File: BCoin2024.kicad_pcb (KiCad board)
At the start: 2 copper layers, 50 x 50 mm, 21 parts, among them U1 NE555DR, U2 74HC4017D_653

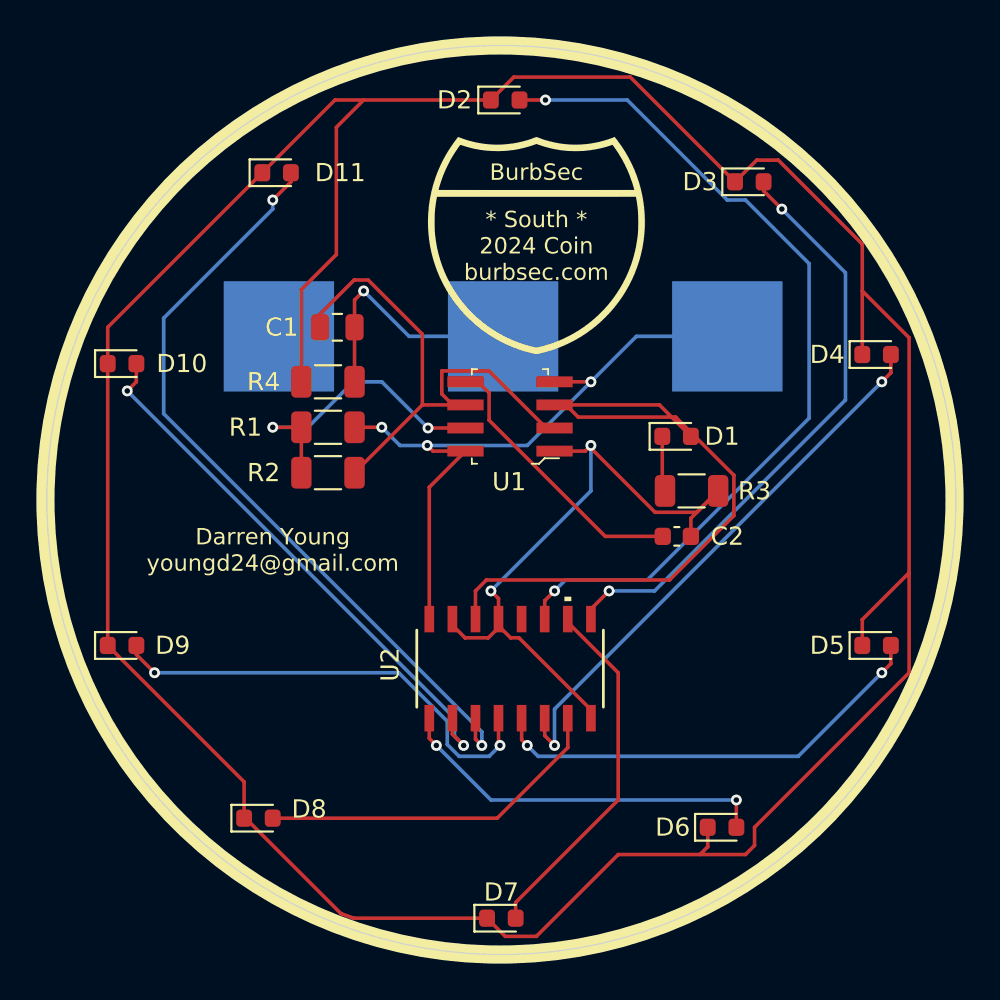
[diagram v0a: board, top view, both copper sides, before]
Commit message: added datasheets
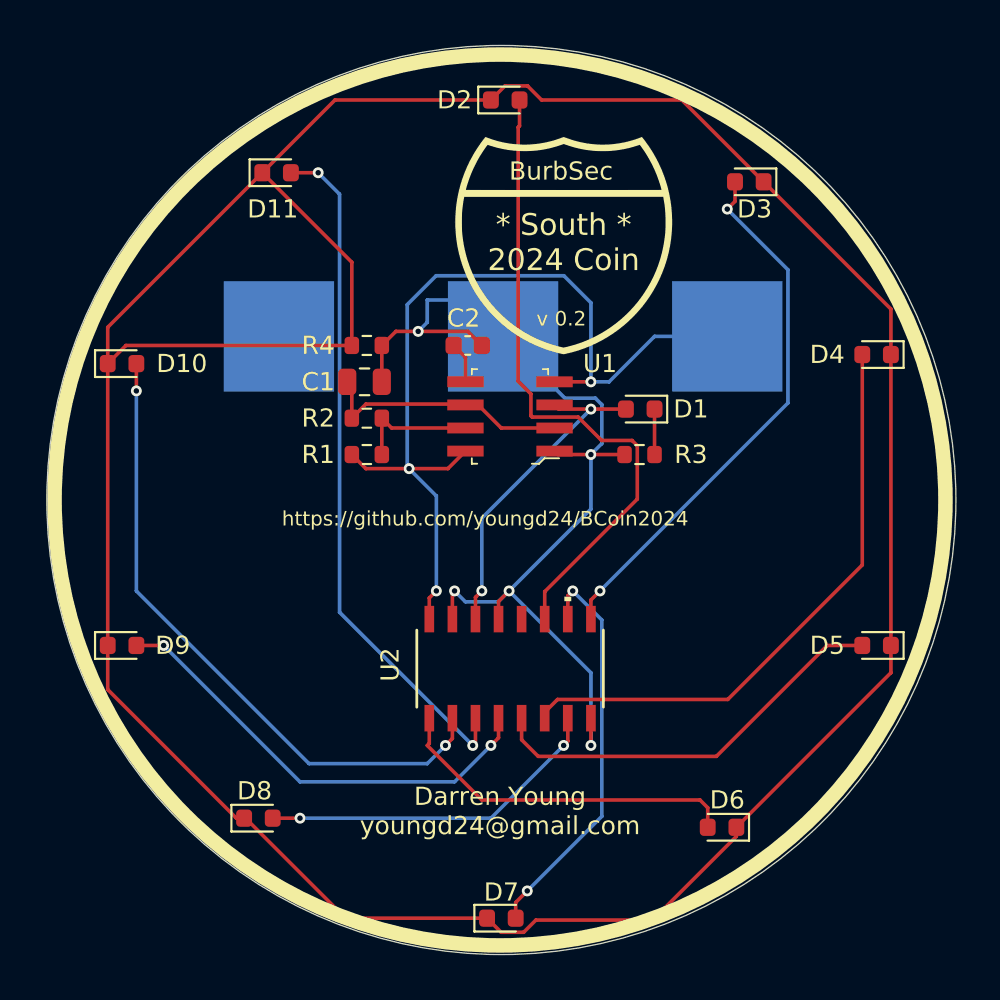
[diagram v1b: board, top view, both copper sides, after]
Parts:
- R1, R2, R3, R4: footprint Resistor_SMD:R_1206_3216Metric -> Resistor_SMD:R_0603_1608Metric
- moved C2 15.6 mm to (132.7, 81.5)
- moved R2 3.68 mm to (127.2, 85.5), turned to 180 degrees
- moved R3 3.49 mm to (142.2, 87.5), turned to 180 degrees
- moved C1 3.35 mm to (127.0, 83.5)
- moved R4 2.93 mm to (127.2, 81.5)
- moved R1 2.61 mm to (127.2, 87.5), turned to 0 degrees
- moved D1 2.50 mm to (142.2, 85.0), turned to 180 degrees
- moved G*** 1.50 mm to (138.0, 76.0)
- turned D3 to 180 degrees
- turned D4 to 180 degrees
- turned D5 to 180 degrees
- turned D6 to 180 degrees
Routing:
- net Net-(D1-A): track 39.4 -> 18.2 mm, vias 0 -> 2
- net Net-(U1-THRES): track 30.2 -> 14.1 mm
- net VCC: track 37.7 -> 51.4 mm
- net Net-(U1-CONT): track 15.3 -> 2.27 mm
- net Net-(D2-A): track 47.9 -> 35.9 mm, vias 2 -> 0
- net Net-(U1-DISCH): track 16.8 -> 6.82 mm, vias 2 -> 0
- net Net-(D10-K): track 179.7 -> 173.6 mm
- net Net-(D11-A): track 43.3 -> 38.1 mm
- net GND: track 51.9 -> 57.1 mm, vias 3 -> 5
- net Net-(D10-A): track 30.6 -> 35.5 mm
- net Net-(D3-A): track 33.2 -> 30.1 mm
- net Net-(D7-A): track 19.9 -> 22.3 mm, vias 0 -> 2
- net Net-(D5-A): track 25.0 -> 22.8 mm, vias 2 -> 0
- net Net-(D4-A): track 30.9 -> 32.7 mm, vias 2 -> 0
- net Net-(D6-A): track 20.9 -> 19.5 mm, vias 2 -> 0
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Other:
- board text added: "* South * 2024 Coin"
- board text added: "https://github.com/youngd24/BCoin2024"
- board text added: "v 0.2"
- board text removed: "* South * 2024 Coin burbsec.com"

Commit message: added assets and images
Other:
- board text added: "v0.2"
- board text removed: "v 0.2"
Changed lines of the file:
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@@
 		)
 	)
-	(gr_text "v 0.2"
+	(gr_text "v0.2"
 		(at 136.5 80.5 0)
 		(layer "F.SilkS")

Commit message: Version 0.3
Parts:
- added C3: 10nF, Capacitor_SMD:C_0603_1608Metric, F.Cu at (142.0, 86.0)
- moved G*** 3.50 mm to (134.5, 76.0)
- moved D1 2.76 mm to (142.0, 87.8)
- moved U2 2.56 mm to (134.8, 96.7)
- moved U1 2.29 mm to (134.6, 87.6)
- moved C1 2.23 mm to (127.0, 85.7)
- moved C2 2.23 mm to (132.7, 83.7)
- moved R2 2.23 mm to (127.2, 87.7)
- moved R4 2.23 mm to (127.2, 83.7)
- moved R3 2.00 mm to (142.1, 89.5)
- moved R1 2.00 mm to (127.2, 89.5)
- moved BT1 1.00 mm to (134.7, 80.0)
- moved D2 0.50 mm to (134.8, 67.5)
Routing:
- net VCC: track 51.4 -> 36.7 mm, vias 3 -> 6
- net Net-(D7-A): track 22.3 -> 31.6 mm
- net Net-(D2-A): track 35.9 -> 29.9 mm, vias 0 -> 2
- net GND: track 57.1 -> 51.4 mm, vias 5 -> 3
- net Net-(D3-A): track 30.1 -> 25.5 mm
- net Net-(D8-A): track 19.3 -> 23.8 mm
- net Net-(D10-A): track 35.5 -> 31.8 mm
- net Net-(D1-A): track 18.2 -> 14.8 mm
- net Net-(D11-A): track 38.1 -> 34.7 mm
- net Net-(D5-A): track 22.8 -> 24.9 mm, vias 0 -> 2
- net Net-(D6-A): track 19.5 -> 21.1 mm, vias 0 -> 2
- net Net-(D9-A): track 25.1 -> 23.9 mm
- net Net-(D10-K): track 173.6 -> 172.6 mm, vias 0 -> 11
- net Net-(U1-DISCH): track 6.82 -> 6.09 mm
- net Net-(U1-THRES): track 14.1 -> 13.6 mm
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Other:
- board text added: "${REVISION}"
- board text added: "2nd Thursday of the month Prime Time Restaurant Hickory Hills 95th St 6:30 PM"
- board text added: "Darren Young youngd24@gmail.com https://github.com/youngd24/BCoin2024"
- board text added: "v0.3"
- board text removed: "Darren Young youngd24@gmail.com"
- board text removed: "https://github.com/youngd24/BCoin2024"
- board text removed: "v0.2"

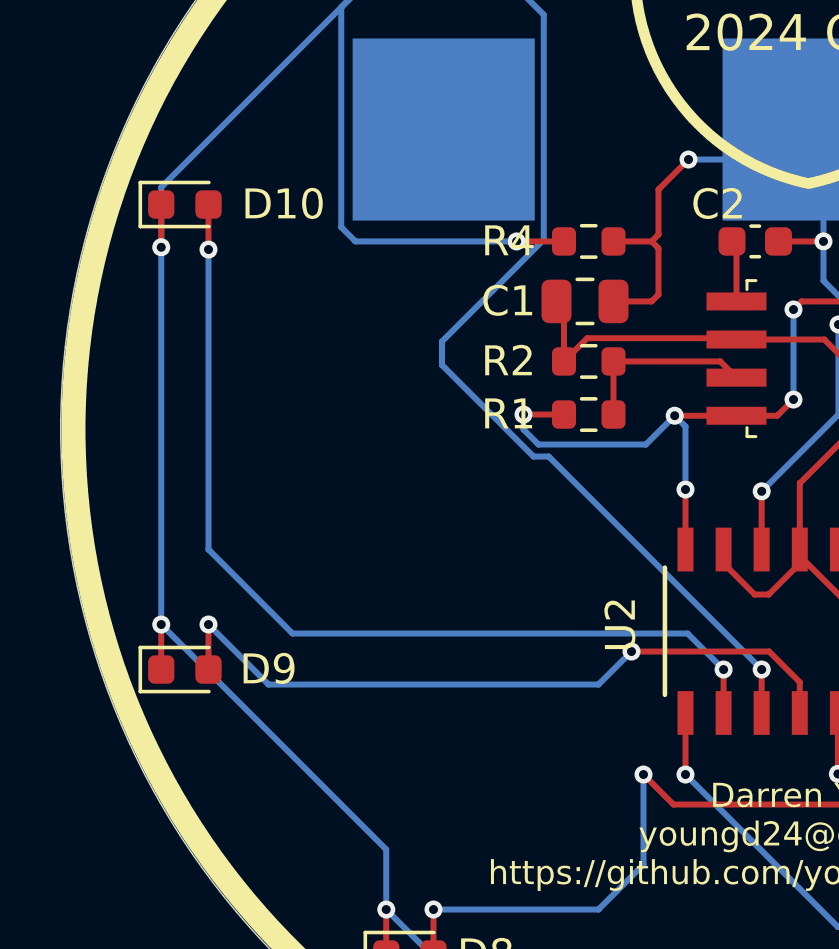
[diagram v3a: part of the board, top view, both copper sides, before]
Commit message: added malort footprint
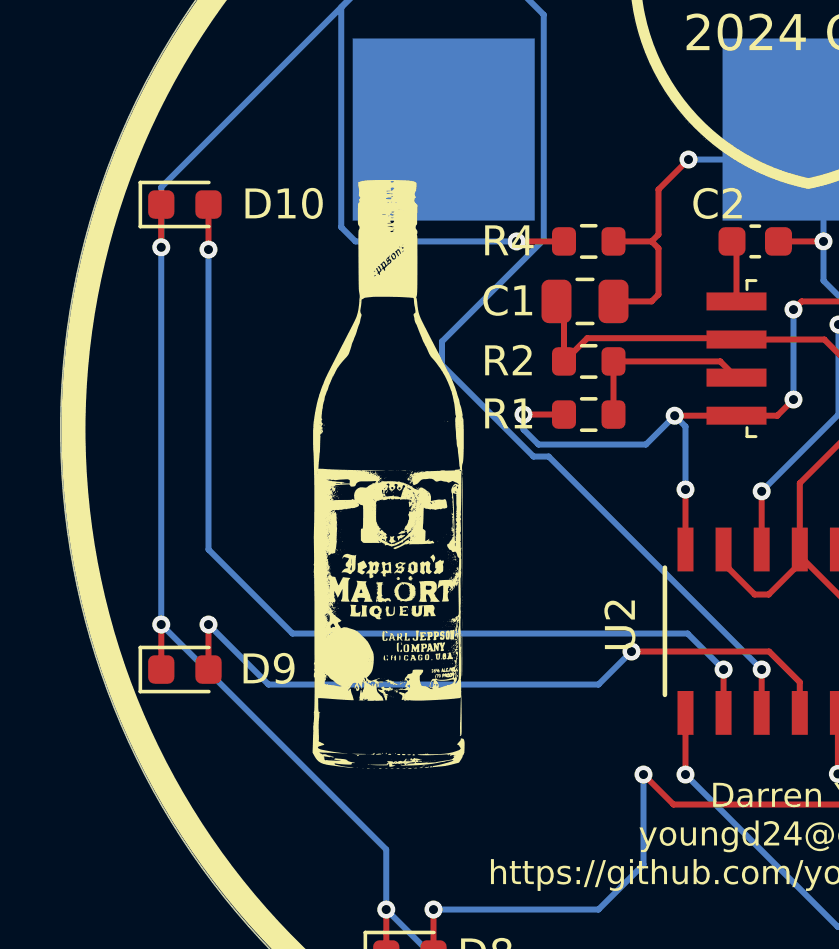
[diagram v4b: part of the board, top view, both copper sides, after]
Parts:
- added G***: LOGO, BCoin_Footprint_Library:malort01, F.Cu at (120.5, 91.5)

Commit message: Adding v0.4 changes
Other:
- board text added: "*"
- board text added: "-"
- board text added: "CR2016 Battery"
- board text added: "GND"
- board text added: "S+1 VCC"
- board text added: "v0.4"
- board text removed: "v0.3"
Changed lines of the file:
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@@
 		(tags "LED")
 		(property "Reference" "D5"
-			(at 2.7125 0 0)
+			(at 0.4625 -1.75 0)
 			(layer "F.SilkS")
 			(effects
@@
 		(tags "LED")
 		(property "Reference" "D4"
-			(at 2.7125 0 0)
+			(at 0.7125 1.75 0)
 			(layer "F.SilkS")
 			(effects
@@
 		(tags "LED")
 		(property "Reference" "D10"
-			(at 3.2875 0 0)
+			(at 0.5375 -1.75 0)
 			(layer "F.SilkS")
 			(effects
@@
 		(tags "LED")
 		(property "Reference" "D9"
-			(at 2.7875 0 0)
+			(at 0.5375 1.75 0)
 			(layer "F.SilkS")
 			(effects
@@
 		(tags "LED")
 		(property "Reference" "D6"
-			(at 2.4625 0 0)
+			(at 0.7125 -1.75 0)
 			(layer "F.SilkS")
 			(effects
@@
 		(tags "LED")
 		(property "Reference" "D8"
-			(at 2.5375 0 0)
+			(at 0.7875 1.75 0)
 			(layer "F.SilkS")
 			(effects
@@
 		(tags "LED")
 		(property "Reference" "D11"
-			(at 3.2875 0 0)
+			(at 1.5375 -1.75 0)
 			(layer "F.SilkS")
 			(effects
@@
 		(tags "LED")
 		(property "Reference" "D3"
-			(at 2.7125 0 0)
+			(at 1.7125 1.75 0)
 			(layer "F.SilkS")
 			(effects
@@
 		(at 134.67 80 180)
 		(property "Reference" "BT1"
-			(at 0.67 9 0)
+			(at 0.17 7.5 0)
 			(layer "B.SilkS")
 			(effects
@@
 		(layer "Edge.Cuts")
 	)
+	(gr_text "S+1\nVCC"
+		(at 148 86.5 0)
+		(layer "B.SilkS")
+		(effects
+			(font
+				(size 1 1)
+				(thickness 0.1)
+			)
+			(justify bottom mirror)
+		)
+	)
+	(gr_text "GND"
+		(at 134.75 85.25 0)
+		(layer "B.SilkS")
+		(effects
+			(font
+				(size 1 1)
+				(thickness 0.1)
+			)
+			(justify bottom mirror)
+		)
+	)
+	(gr_text "CR2016 Battery"
+		(at 134.5 71 0)
+		(layer "B.SilkS")
+		(effects
+			(font
+				(size 1 1)
+				(thickness 0.125)
+			)
+			(justify bottom mirror)
+		)
+	)
 	(gr_text "2nd Thursday of the month\nPrime Time Restaurant\nHickory Hills\n95th St\n6:30 PM"
 		(at 134.5 107.5 0)
@@
 		)
 	)
+	(gr_text "-"
+		(at 112 84.25 0)
+		(layer "F.SilkS")
+		(effects
+			(font
+				(size 1 0.8)
+				(thickness 0.1)
+			)
+			(justify bottom)
+		)
+	)
 	(gr_text "Darren Young\nyoungd24@gmail.com\nhttps://github.com/youngd24/BCoin2024"
 		(at 135 105.25 0)
@@
 		)
 	)
-	(gr_text "v0.3"
+	(gr_text "-"
+		(at 119 108 0)
+		(layer "F.SilkS")
+		(effects
+			(font
+				(size 1 0.8)
+				(thickness 0.1)
+			)
+			(justify bottom)
+		)
+	)
+	(gr_text "-"
+		(at 150.25 74 0)
+		(layer "F.SilkS")
+		(effects
+			(font
+				(size 1 0.8)
+				(thickness 0.1)
+			)
+			(justify bottom)
+		)
+	)
+	(gr_text "*"
+		(at 138 91.25 0)
+		(layer "F.SilkS")
+		(effects
+			(font
+				(size 1 0.8)
+				(thickness 0.1)
+			)
+			(justify left bottom)
+		)
+	)
+	(gr_text "v0.4"
 		(at 133 111 0)
 		(layer "F.SilkS")
@@
 		)
 	)
+	(gr_text "-"
+		(at 120 73.5 0)
+		(layer "F.SilkS")
+		(effects
+			(font
+				(size 1 0.8)
+				(thickness 0.1)
+			)
+			(justify bottom)
+		)
+	)
+	(gr_text "-"
+		(at 132 69 0)
+		(layer "F.SilkS")
+		(effects
+			(font
+				(size 1 0.8)
+				(thickness 0.1)
+			)
+			(justify bottom)
+		)
+	)
 	(gr_text "BurbSec"
 		(at 131.5 72.5 0)
@@
 		)
 	)
+	(gr_text "-"
+		(at 132.25 112.5 0)
+		(layer "F.SilkS")
+		(effects
+			(font
+				(size 1 0.8)
+				(thickness 0.1)
+			)
+			(justify bottom)
+		)
+	)
+	(gr_text "-"
+		(at 157 83.75 0)
+		(layer "F.SilkS")
+		(effects
+			(font
+				(size 1 0.8)
+				(thickness 0.1)
+			)
+			(justify bottom)
+		)
+	)
+	(gr_text "-"
+		(at 112 97.25 0)
+		(layer "F.SilkS")
+		(effects
+			(font
+				(size 1 0.8)
+				(thickness 0.1)
+			)
+			(justify bottom)
+		)
+	)
+	(gr_text "-"
+		(at 156.6975 97.265 0)
+		(layer "F.SilkS")
+		(effects
+			(font
+				(size 1 0.8)
+				(thickness 0.1)
+			)
+			(justify bottom)
+		)
+	)
+	(gr_text "-"
+		(at 148.75 108.5 0)
+		(layer "F.SilkS")
+		(effects
+			(font
+				(size 1 0.8)
+				(thickness 0.1)
+			)
+			(justify bottom)
+		)
+	)
 	(gr_text "* South *\n2024 Coin"
 		(at 134.5 77.5 0)
@@
 				(thickness 0.1)
 			)
+			(justify bottom)
+		)
+	)
+	(gr_text "*"
+		(at 129.5 101.5 0)
+		(layer "F.SilkS")
+		(effects
+			(font
+				(size 1 0.8)
+				(thickness 0.1)
+			)
